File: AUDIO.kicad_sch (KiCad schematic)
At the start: 31 parts, among them J9 AudioJack, U9 ES8388

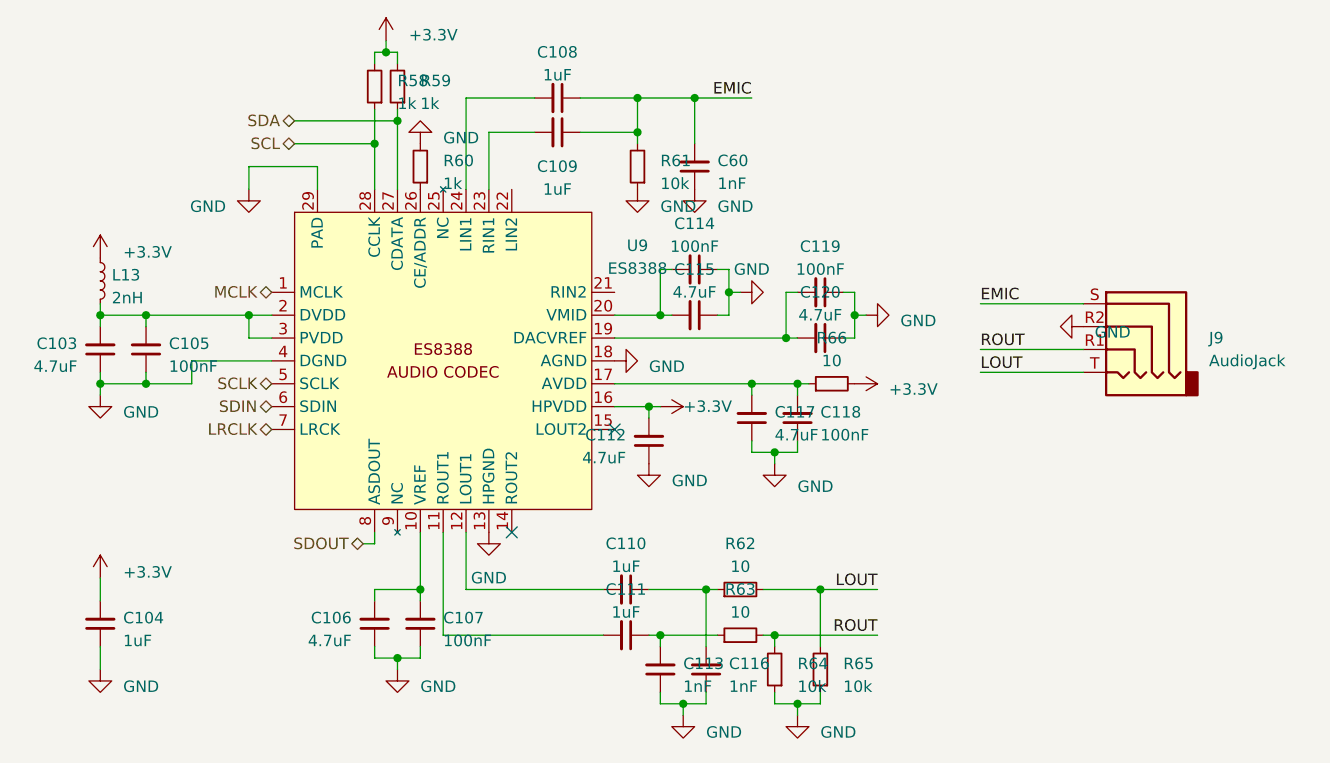
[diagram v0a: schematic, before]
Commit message: Fix USB silkscreen name.
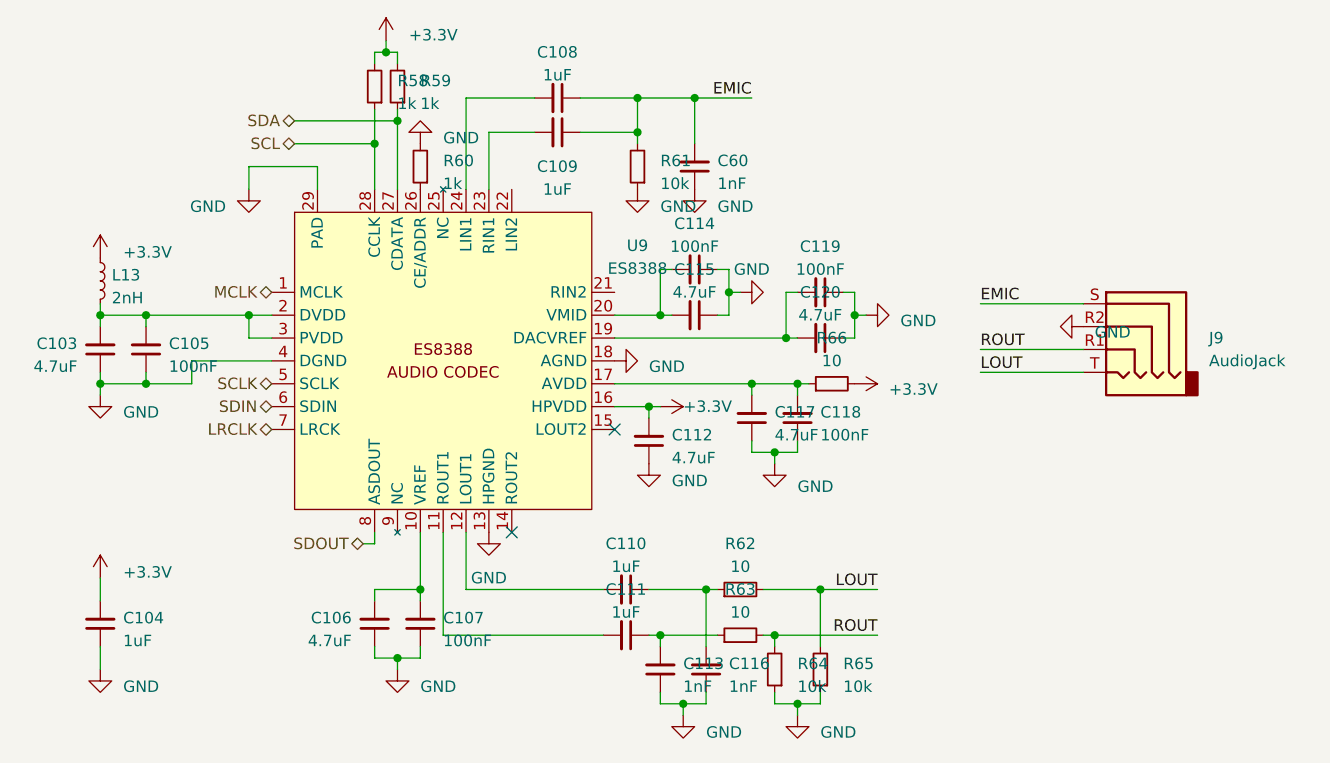
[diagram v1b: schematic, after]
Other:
- moved on the sheet: C112
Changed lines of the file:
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@@
     )
   )
-  (symbol (lib_id "Device:C_Small") (at 116.84 67.31 180) (unit 1)
-    (in_bom yes) (on_board yes) (dnp no) (fields_autoplaced)
-    (property "Reference" "C112" (at 114.3 66.6686 0)
+  (symbol (lib_id "Device:C_Small") (at 116.84 67.31 0) (mirror x) (unit 1)
+    (in_bom yes) (on_board yes) (dnp no)
+    (property "Reference" "C112" (at 119.38 66.6686 0)
       (effects (font (size 1.27 1.27)) (justify left))
     )
-    (property "Value" "4.7uF" (at 114.3 69.2086 0)
+    (property "Value" "4.7uF" (at 119.38 69.2086 0)
       (effects (font (size 1.27 1.27)) (justify left))
     )
